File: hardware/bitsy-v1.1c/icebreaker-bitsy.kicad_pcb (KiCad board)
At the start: 4 copper layers, 36 x 18 mm, 106 parts, among them J1 USB_C, P0 0, P1 1, P10 10, P11 11, P12 12, P13 13, P14 14, P15 15, P16 16, P17 17, P18 18, P19 19, P2 2, P20 20, P21 21, P22 22, P23 23, P24 GND, P25 GND, P26 GND, P27 3V3, P28 3V3, P29 VIN, P3 3, P30 CDONE, P31 CRESET, P32 UP, P33 UP, P34 UP, P35 UP, P36 CS, P37 SCK, P38 CIPO, P39 COPI, P4 4, P40 IO3, P41 IO2, P5 5, P6 6, P7 7, P8 8, P9 9, SW1 TACT, U1 USBLC6-2, U2 TLV75533PDRV, U3 TLV73312PDRV, U4 LY68L6400, U5 W25Q128JVxxM, U6 ICE40UP5K-SG48, X1 12MHz

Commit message: Adding JLCPCB
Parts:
- added C12: 100n, Capacitor_SMD:C_0402_1005Metric, F.Cu at (3.85, 0.48)
- added R12: 2k2, Resistor_SMD:R_0402_1005Metric, F.Cu at (0.95, 2.48)
- added R13: 2k2, Resistor_SMD:R_0402_1005Metric, F.Cu at (0.95, 4.47)
- added R5: 22E, Resistor_SMD:R_0402_1005Metric, F.Cu at (0.95, 0.49)
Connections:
- D2 pad A: Net-(R12-Pad1) -> Net-(D2-PadA)

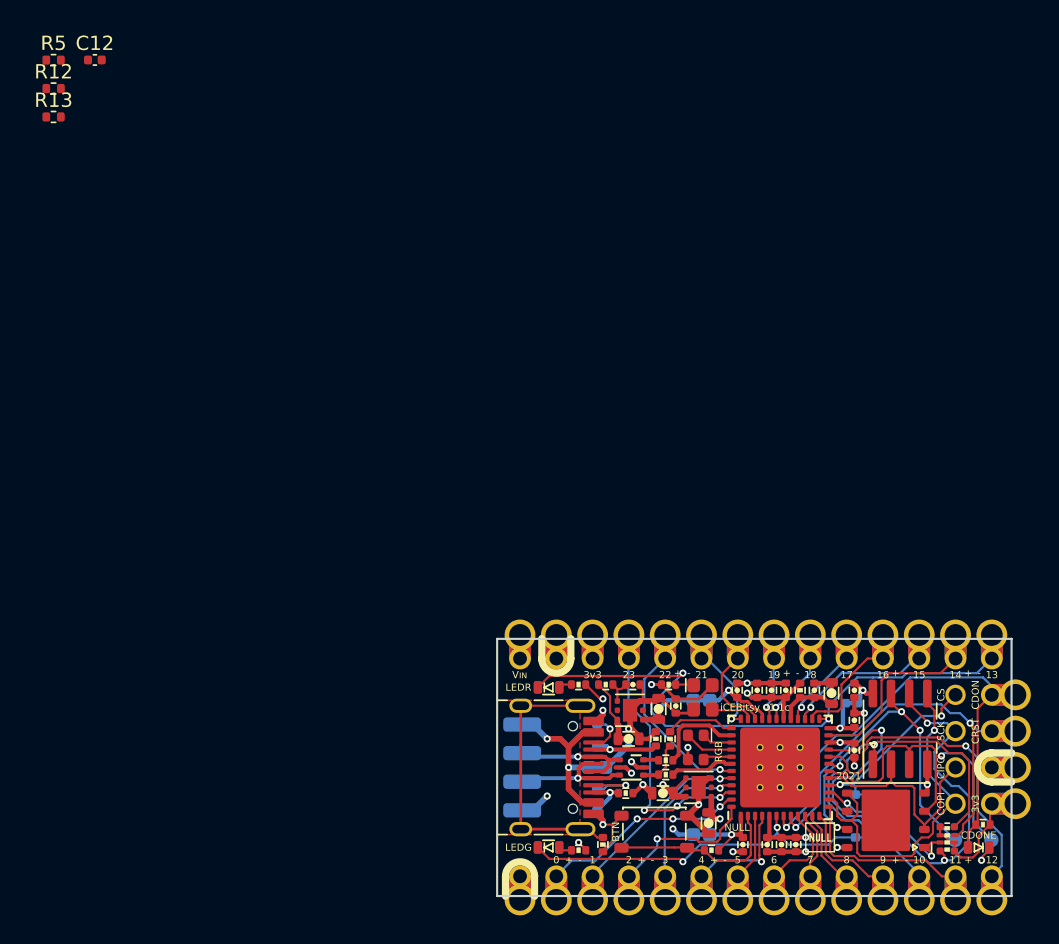
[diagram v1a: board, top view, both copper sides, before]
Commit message: changed some 0402 to use the regular library in Kicad v9
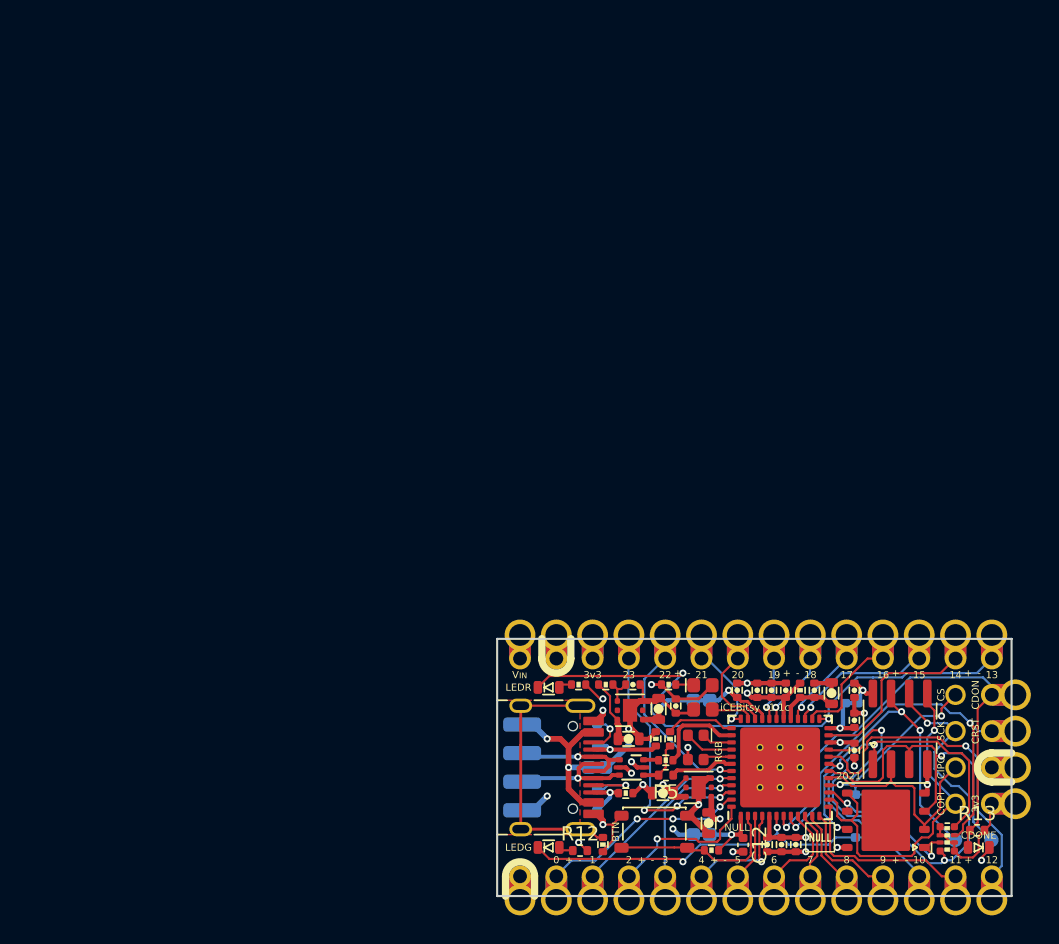
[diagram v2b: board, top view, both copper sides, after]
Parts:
- removed the C12 at (49.2, 55.4)
- removed the C12 at (3.85, 0.48)
- removed the R12 at (37.7, 55.8)
- removed the R12 at (0.95, 2.48)
- removed the R13 at (66.0, 54.0)
- removed the R13 at (0.95, 4.47)
- removed the R5 at (43.8, 50.5)
- removed the R5 at (0.95, 0.49)
- added C12: 100n, Capacitor_SMD:C_0402_1005Metric, F.Cu at (49.2, 55.4)
- added R12: 2k2, Resistor_SMD:R_0402_1005Metric, F.Cu at (37.8, 55.8)
- added R13: 2k2, Resistor_SMD:R_0402_1005Metric, F.Cu at (65.6, 54.4)
- added R5: 22E, Resistor_SMD:R_0402_1005Metric, F.Cu at (43.8, 50.5)
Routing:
- net Net-(R12-Pad1): track 0.93 -> 0.00 mm
- net Net-(D2-PadA): track 0.00 -> 0.93 mm

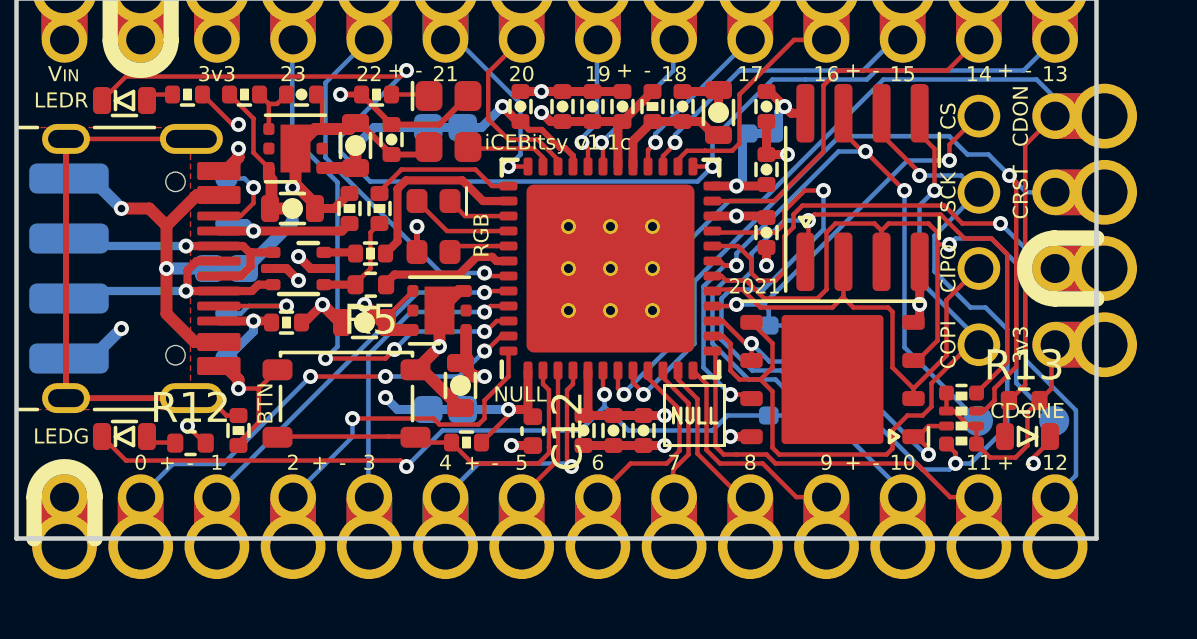
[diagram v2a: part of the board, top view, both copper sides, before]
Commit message: PCB changes for JLCPCB parts made.
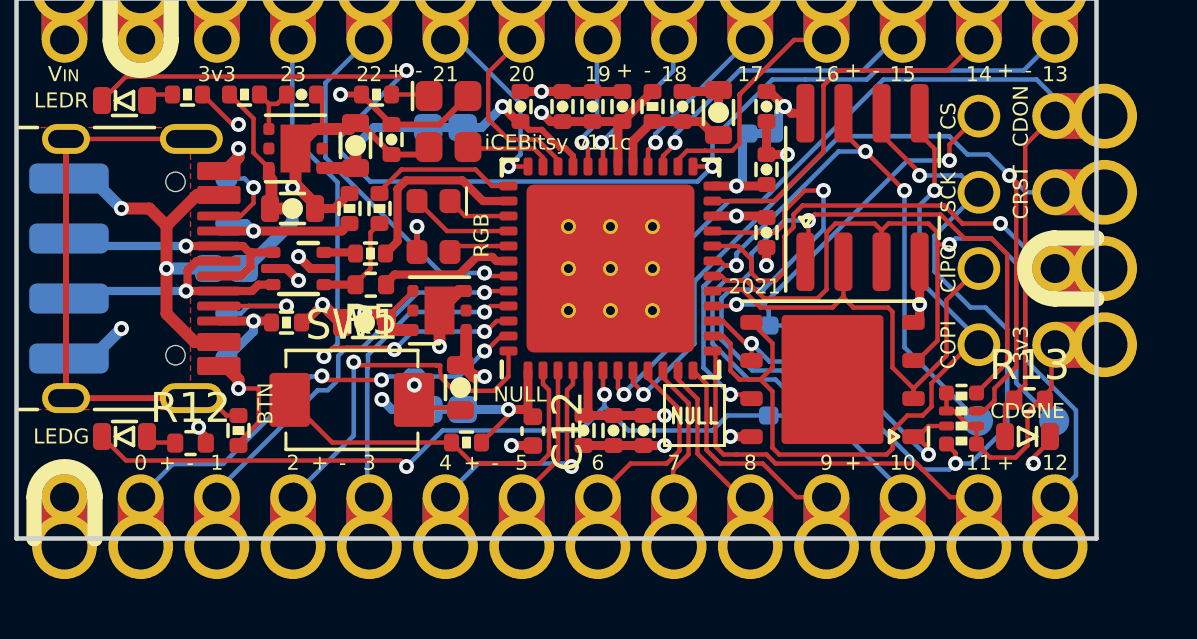
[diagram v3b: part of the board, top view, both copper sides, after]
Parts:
- SW1: footprint pkl_buttons_switches:SW_SPST_3x4x2.5 -> SWitch:TS-1088-AR02016
- moved SW1 0.22 mm to (43.2, 54.4), turned to 90 degrees
- moved R13 0.18 mm to (65.8, 54.4)
- moved C5 0.07 mm to (46.8, 54.0)
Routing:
- net +3V3: track 29.5 -> 36.0 mm
- net /IOB_4a: track 10.6 -> 12.1 mm
- net GND: track 41.4 -> 40.7 mm, vias 15 -> 16
